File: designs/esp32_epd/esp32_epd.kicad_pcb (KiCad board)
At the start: 2 copper layers, 23.9 x 50.8 mm, 8 parts, among them J1 Conn_01x12, J2 Conn_01x16, J3 XF2M-2415-1A

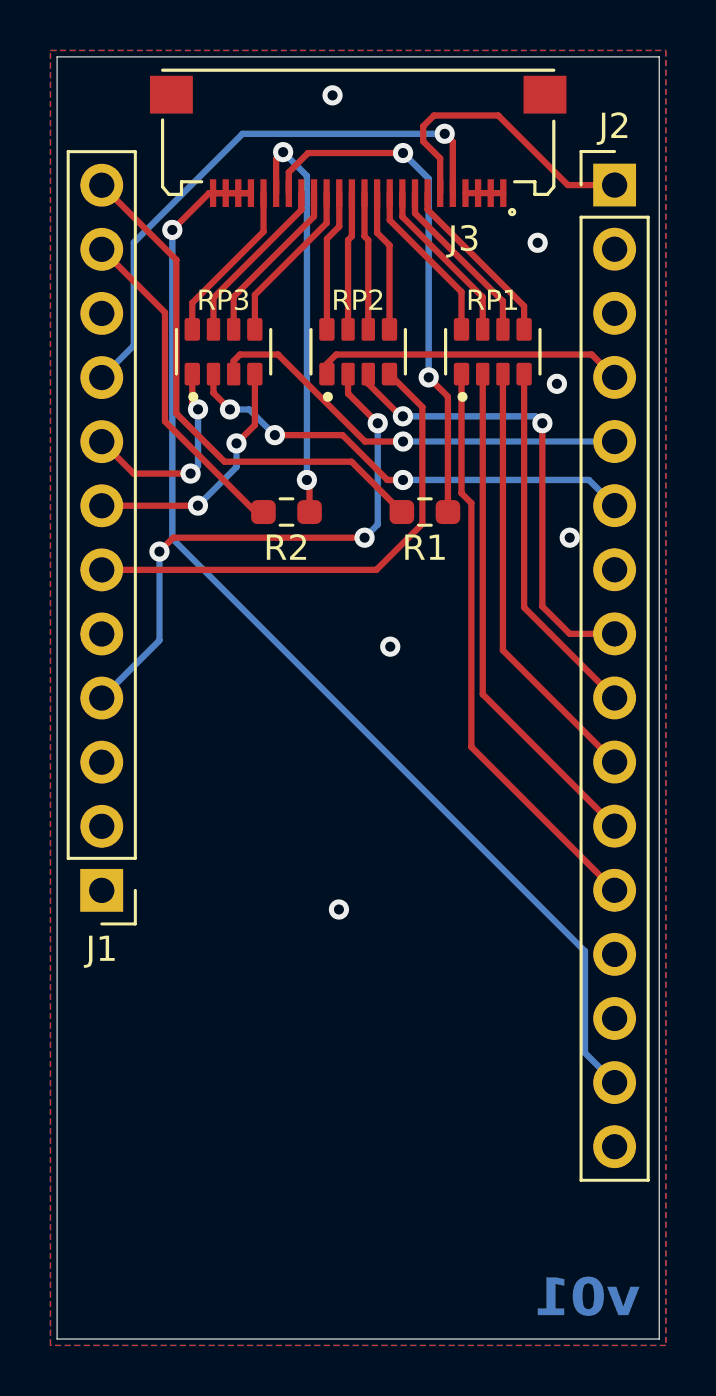
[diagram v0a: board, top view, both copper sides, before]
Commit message: Fix PCB sch and layout with VCC->VBAT
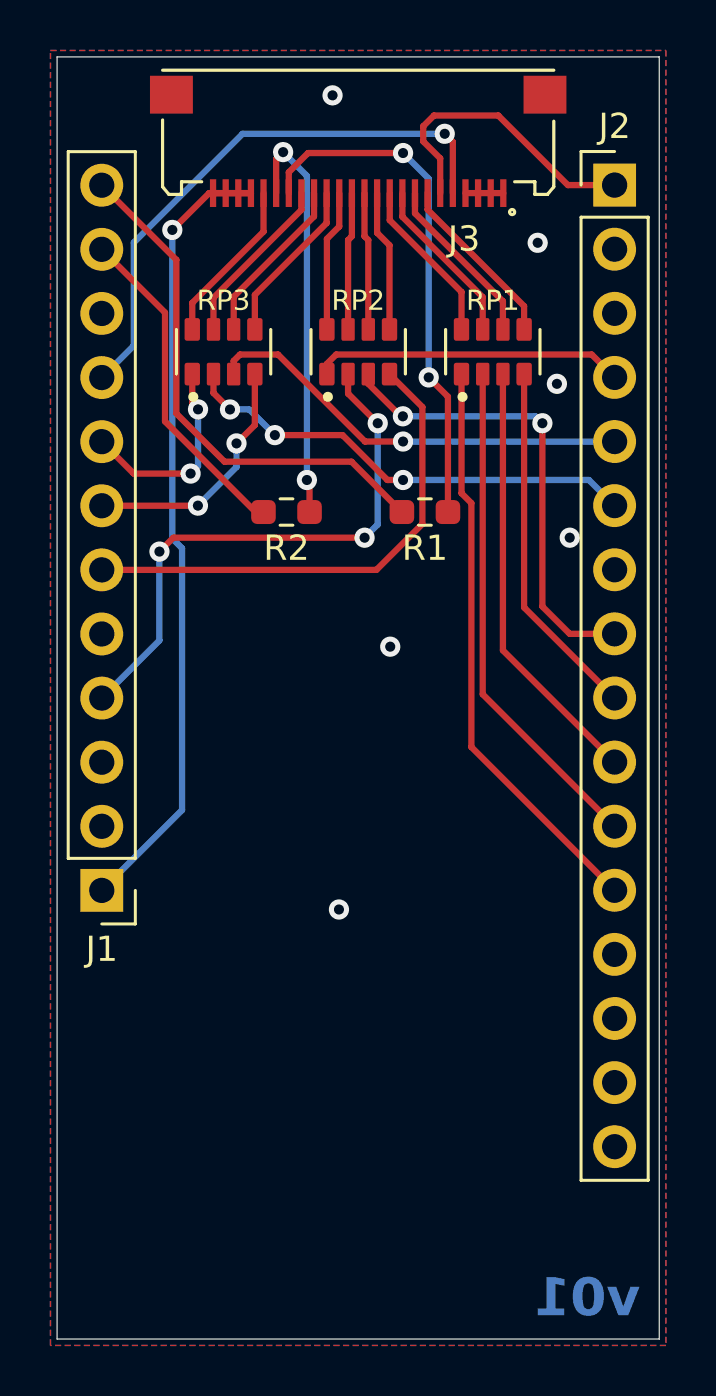
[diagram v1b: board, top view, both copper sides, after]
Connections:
- J1 pad 1: /VBAT -> VCC
- J2 pad 15: VCC -> unconnected-(J2-Pin_15-Pad15)
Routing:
- net VCC: track 46.3 -> 32.9 mm
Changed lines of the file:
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@@
   (net 31 "/I2C_SCL")
   (net 32 "/HD{slash}C")
-  (net 33 "/VBAT")
+  (net 33 "unconnected-(J2-Pin_15-Pad15)")
   (net 34 "/EN")
   (net 35 "/USB")
@@
       (stroke (width 0.1) (type solid)) (layer "F.Fab"))
     (pad "1" thru_hole rect (at 0 0 180) (size 1.7 1.7) (drill 1) (layers "*.Cu" "*.Mask")
-      (net 33 "/VBAT") (pinfunction "Pin_1") (pintype "passive"))
+      (net 18 "VCC") (pinfunction "Pin_1") (pintype "passive"))
     (pad "2" thru_hole oval (at 0 2.54 180) (size 1.7 1.7) (drill 1) (layers "*.Cu" "*.Mask")
       (net 34 "/EN") (pinfunction "Pin_2") (pintype "passive"))
@@
       (net 40 "/NC") (pinfunction "Pin_14") (pintype "passive"))
     (pad "15" thru_hole oval (at 0 35.56) (size 1.7 1.7) (drill 1) (layers "*.Cu" "*.Mask")
-      (net 18 "VCC") (pinfunction "Pin_15") (pintype "passive"))
+      (net 33 "unconnected-(J2-Pin_15-Pad15)") (pinfunction "Pin_15") (pintype "passive"))
     (pad "16" thru_hole oval (at 0 38.1) (size 1.7 1.7) (drill 1) (layers "*.Cu" "*.Mask")
       (net 41 "/RESET") (pinfunction "Pin_16") (pintype "passive"))
@@
   (segment (start 81.724 56.198) (end 80.265799 57.656201) (width 0.25) (layer "F.Cu") (net 18))
   (via (at 80.265799 57.656201) (size 0.8) (drill 0.4) (layers "F.Cu" "B.Cu") (net 18))
+  (segment (start 77.47 83.825) (end 80.6514 80.6436) (width 0.25) (layer "B.Cu") (net 18))
+  (segment (start 80.6514 80.6436) (end 80.6514 70.270595) (width 0.25) (layer "B.Cu") (net 18))
+  (segment (start 80.6514 70.270595) (end 80.265799 69.884994) (width 0.25) (layer "B.Cu") (net 18))
   (segment (start 80.265799 57.656201) (end 80.265799 69.884994) (width 0.25) (layer "B.Cu") (net 18))
-  (segment (start 96.615 90.265) (end 97.79 91.44) (width 0.25) (layer "B.Cu") (net 18))
-  (segment (start 80.265799 69.884994) (end 96.615 86.234195) (width 0.25) (layer "B.Cu") (net 18))
-  (segment (start 96.615 86.234195) (end 96.615 90.265) (width 0.25) (layer "B.Cu") (net 18))
   (segment (start 90.38 56.852) (end 90.38 56.198) (width 0.25) (layer "F.Cu") (net 19))
   (segment (start 94.204 60.676) (end 90.38 56.852) (width 0.25) (layer "F.Cu") (net 19))
